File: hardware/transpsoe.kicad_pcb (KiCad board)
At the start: 2 copper layers, 102.2 x 51 mm, 107 parts, among them J1 AudioJack2_SwitchT, J10 AudioJack2_SwitchT, J11 AudioJack2_SwitchT, J12 Conn_01x08_Female, J13 Conn_01x08_Female, J14 Conn_01x08_Male, J15 Conn_01x08_Male, J2 AudioJack2_SwitchT, J3 AudioJack2_SwitchT, J4 AudioJack2_SwitchT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

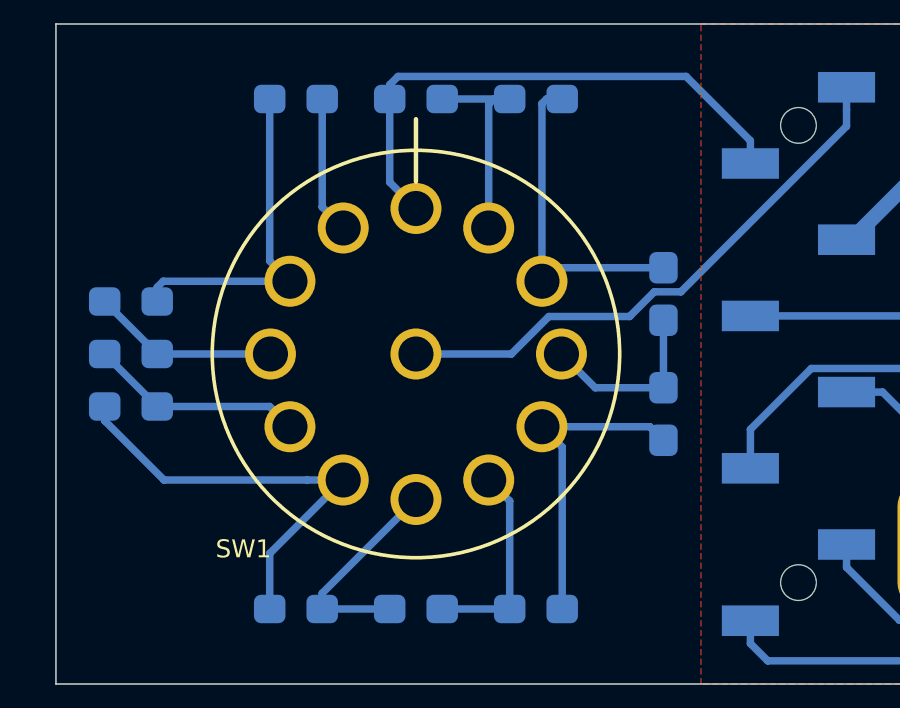
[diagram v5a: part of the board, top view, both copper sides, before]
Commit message: Increase annular ring size on rotary switch
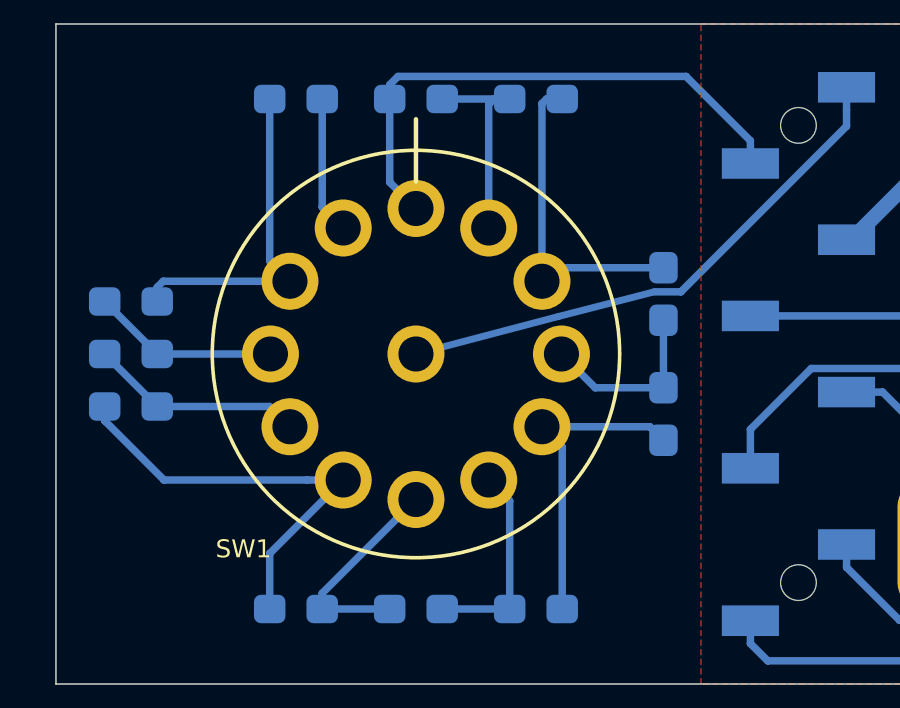
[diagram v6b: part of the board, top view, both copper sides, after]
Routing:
- net Jacks-SW1.a: track 18.8 -> 18.2 mm
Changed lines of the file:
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@@
     (thickness 1.6)
     (drawings 12)
-    (tracks 918)
+    (tracks 916)
     (zones 0)
     (modules 107)
@@
   )
   (setup
-    (last_trace_width 0.5)
+    (last_trace_width 0.25)
+    (user_trace_width 0.23)
     (user_trace_width 0.25)
     (user_trace_width 0.5)
@@
     (add_net SW1.b)
   )
+  (module transpsoe:MC12xxxCxx (layer F.Cu)
+    (at 112 111.25)
+    (descr "Half-inch Rotary Switch")
+    (fp_text reference SW1 (at -5.75 6.5) (layer F.SilkS)
+      (effects (font (size 0.6 0.6) (thickness 0.127)))
+    )
+    (fp_text value SW_Rotary12 (at 0 -9.25) (layer F.Fab)
+      (effects (font (size 1 1) (thickness 0.15)))
+    )
+    (fp_circle (center 0 0) (end -1.726323 -6.442725) (layer F.Fab) (width 0.1))
+    (fp_circle (center 0 0) (end -1.757381 -6.558636) (layer F.SilkS) (width 0.12))
+    (fp_circle (center 0 0) (end -1.822086 -6.800118) (layer F.CrtYd) (width 0.05))
+    (fp_line (start 0 -5.75) (end 0 -7.826787) (layer F.SilkS) (width 0.15))
+    (pad 1 thru_hole oval (at 0 -4.85 90) (size 1.9 1.9) (drill 1.17) (layers *.Cu *.Mask)
+      (net 78 Jacks-SW1.b))
+    (pad 2 thru_hole oval (at 2.424999 -4.200223 90) (size 1.9 1.9) (drill 1.17) (layers *.Cu *.Mask)
+      (net 47 "Net-(R81-Pad2)"))
+    (pad 3 thru_hole oval (at 4.200223 -2.425 90) (size 1.9 1.9) (drill 1.17) (layers *.Cu *.Mask)
+      (net 46 "Net-(R80-Pad2)"))
+    (pad 4 thru_hole oval (at 4.85 0 90) (size 1.9 1.9) (drill 1.17) (layers *.Cu *.Mask)
+      (net 45 "Net-(R79-Pad2)"))
+    (pad 5 thru_hole oval (at 4.200223 2.424999 90) (size 1.9 1.9) (drill 1.17) (layers *.Cu *.Mask)
+      (net 44 "Net-(R78-Pad2)"))
+    (pad 6 thru_hole oval (at 2.424999 4.200223 90) (size 1.9 1.9) (drill 1.17) (layers *.Cu *.Mask)
+      (net 43 "Net-(R77-Pad2)"))
+    (pad 7 thru_hole oval (at 0 4.85 90) (size 1.9 1.9) (drill 1.17) (layers *.Cu *.Mask)
+      (net 42 "Net-(R76-Pad2)"))
+    (pad 8 thru_hole oval (at -2.425 4.200223 90) (size 1.9 1.9) (drill 1.17) (layers *.Cu *.Mask)
+      (net 41 "Net-(R75-Pad2)"))
+    (pad 9 thru_hole oval (at -4.200223 2.425 90) (size 1.9 1.9) (drill 1.17) (layers *.Cu *.Mask)
+      (net 40 "Net-(R74-Pad2)"))
+    (pad 10 thru_hole oval (at -4.85 0 90) (size 1.9 1.9) (drill 1.17) (layers *.Cu *.Mask)
+      (net 39 "Net-(R73-Pad2)"))
+    (pad 11 thru_hole oval (at -4.200223 -2.425 90) (size 1.9 1.9) (drill 1.17) (layers *.Cu *.Mask)
+      (net 38 "Net-(R72-Pad2)"))
+    (pad 12 thru_hole oval (at -2.425 -4.200223 90) (size 1.9 1.9) (drill 1.17) (layers *.Cu *.Mask)
+      (net 37 "Net-(R72-Pad1)"))
+    (pad 13 thru_hole oval (at 0 0 90) (size 1.9 1.9) (drill 1.17) (layers *.Cu *.Mask)
+      (net 79 Jacks-SW1.a))
+    (model :transpsoe:MC12L1NCQD.stp
+      (offset (xyz 0 0 2.75))
+      (scale (xyz 1 1 1))
+      (rotate (xyz -90 0 0))
+    )
+  )
   (module Potentiometer_THT:Potentiometer_Bourns_3296W_Vertical (layer B.Cu)
     (at 133 90.25 180)
@@
     )
   )
-  (module transpsoe:MC12xxxCxx (layer F.Cu)
-    (at 112 111.25)
-    (descr "Half-inch Rotary Switch")
-    (fp_text reference SW1 (at -5.75 6.5) (layer F.SilkS)
-      (effects (font (size 0.6 0.6) (thickness 0.127)))
-    )
-    (fp_text value SW_Rotary12 (at 0 -9.25) (layer F.Fab)
-      (effects (font (size 1 1) (thickness 0.15)))
-    )
-    (fp_line (start 0 -5.75) (end 0 -7.826787) (layer F.SilkS) (width 0.15))
-    (fp_circle (center 0 0) (end -1.822086 -6.800118) (layer F.CrtYd) (width 0.05))
-    (fp_circle (center 0 0) (end -1.757381 -6.558636) (layer F.SilkS) (width 0.12))
-    (fp_circle (center 0 0) (end -1.726323 -6.442725) (layer F.Fab) (width 0.1))
-    (pad 13 thru_hole oval (at 0 0 285) (size 1.7 1.7) (drill 1.17) (layers *.Cu *.Mask)
-      (net 79 Jacks-SW1.a))
-    (pad 12 thru_hole oval (at -2.425 -4.200223 90) (size 1.7 1.7) (drill 1.17) (layers *.Cu *.Mask)
-      (net 37 "Net-(R72-Pad1)"))
-    (pad 11 thru_hole oval (at -4.200223 -2.425 90) (size 1.7 1.7) (drill 1.17) (layers *.Cu *.Mask)
-      (net 38 "Net-(R72-Pad2)"))
-    (pad 10 thru_hole oval (at -4.85 0 90) (size 1.7 1.7) (drill 1.17) (layers *.Cu *.Mask)
-      (net 39 "Net-(R73-Pad2)"))
-    (pad 9 thru_hole oval (at -4.200223 2.425 90) (size 1.7 1.7) (drill 1.17) (layers *.Cu *.Mask)
-      (net 40 "Net-(R74-Pad2)"))
-    (pad 8 thru_hole oval (at -2.425 4.200223 90) (size 1.7 1.7) (drill 1.17) (layers *.Cu *.Mask)
-      (net 41 "Net-(R75-Pad2)"))
-    (pad 7 thru_hole oval (at 0 4.85 90) (size 1.7 1.7) (drill 1.17) (layers *.Cu *.Mask)
-      (net 42 "Net-(R76-Pad2)"))
-    (pad 6 thru_hole oval (at 2.424999 4.200223 90) (size 1.7 1.7) (drill 1.17) (layers *.Cu *.Mask)
-      (net 43 "Net-(R77-Pad2)"))
-    (pad 5 thru_hole oval (at 4.200223 2.424999 90) (size 1.7 1.7) (drill 1.17) (layers *.Cu *.Mask)
-      (net 44 "Net-(R78-Pad2)"))
-    (pad 4 thru_hole oval (at 4.85 0 90) (size 1.7 1.7) (drill 1.17) (layers *.Cu *.Mask)
-      (net 45 "Net-(R79-Pad2)"))
-    (pad 3 thru_hole oval (at 4.200223 -2.425 90) (size 1.7 1.7) (drill 1.17) (layers *.Cu *.Mask)
-      (net 46 "Net-(R80-Pad2)"))
-    (pad 2 thru_hole oval (at 2.424999 -4.200223 90) (size 1.7 1.7) (drill 1.17) (layers *.Cu *.Mask)
-      (net 47 "Net-(R81-Pad2)"))
-    (pad 1 thru_hole oval (at 0 -4.85 90) (size 1.7 1.7) (drill 1.17) (layers *.Cu *.Mask)
-      (net 78 Jacks-SW1.b))
-    (model :transpsoe:MC12L1NCQD.stp
-      (offset (xyz 0 0 2.75))
-      (scale (xyz 1 1 1))
-      (rotate (xyz -90 0 0))
-    )
-  )
   (module transpsoe:raccoon-7.5 (layer B.Cu)
     (at 198.2 81.85 180)
@@
   (segment (start 108.875 106.349777) (end 109.575 107.049777) (width 0.25) (layer B.Cu) (net 37))
   (segment (start 108.875 102.75) (end 108.875 106.349777) (width 0.25) (layer B.Cu) (net 37))
-  (segment (start 107.125 108.150223) (end 107.799777 108.825) (width 0.25) (layer B.Cu) (net 38))
-  (segment (start 107.125 102.75) (end 107.125 108.150223) (width 0.25) (layer B.Cu) (net 38))
   (segment (start 103.575 108.825) (end 103.375 109.025) (width 0.25) (layer B.Cu) (net 38))
   (segment (start 103.375 109.025) (end 103.375 109.5) (width 0.25) (layer B.Cu) (net 38))
   (segment (start 107.799777 108.825) (end 103.575 108.825) (width 0.25) (layer B.Cu) (net 38))
+  (segment (start 107.125 108.150223) (end 107.799777 108.825) (width 0.25) (layer B.Cu) (net 38))
+  (segment (start 107.125 102.75) (end 107.125 108.150223) (width 0.25) (layer B.Cu) (net 38))
   (segment (start 101.625 109.5) (end 103.375 111.25) (width 0.25) (layer B.Cu) (net 39))
   (segment (start 103.375 111.25) (end 107.15 111.25) (width 0.25) (layer B.Cu) (net 39))
@@
   (segment (start 120.831912 109.17741) (end 126.3525 103.656822) (width 0.25) (layer B.Cu) (net 79))
   (segment (start 119.944396 109.17741) (end 120.831912 109.17741) (width 0.25) (layer B.Cu) (net 79))
-  (segment (start 119.121806 110) (end 119.944396 109.17741) (width 0.25) (layer B.Cu) (net 79))
-  (segment (start 116.431446 110) (end 119.121806 110) (width 0.25) (layer B.Cu) (net 79))
-  (segment (start 115.181446 111.25) (end 116.431446 110) (width 0.25) (layer B.Cu) (net 79))
-  (segment (start 112 111.25) (end 115.181446 111.25) (width 0.25) (layer B.Cu) (net 79))
+  (segment (start 112 111.25) (end 116.75 110) (width 0.23) (layer B.Cu) (net 79))
+  (segment (start 116.75 110) (end 119.944396 109.17741) (width 0.23) (layer B.Cu) (net 79))
   (segment (start 153.25 110.3) (end 153.25 110.5) (width 0.25) (layer B.Cu) (net 80))
   (segment (start 151 110.3) (end 153.25 110.3) (width 0.25) (layer B.Cu) (net 80))

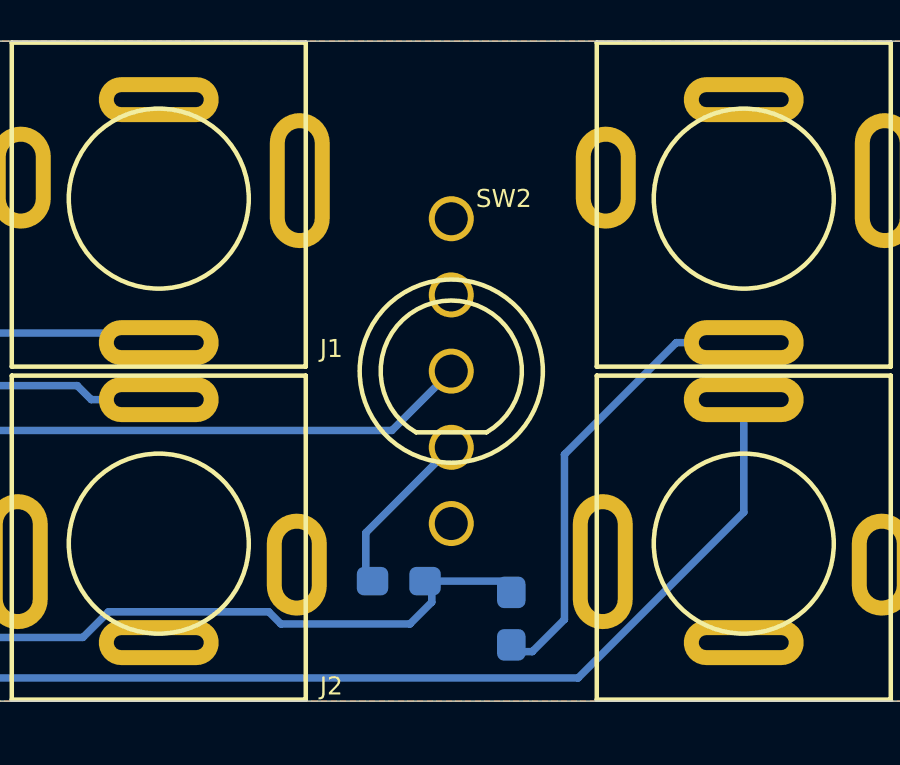
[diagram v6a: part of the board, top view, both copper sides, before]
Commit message: Correct orientation of summing switch
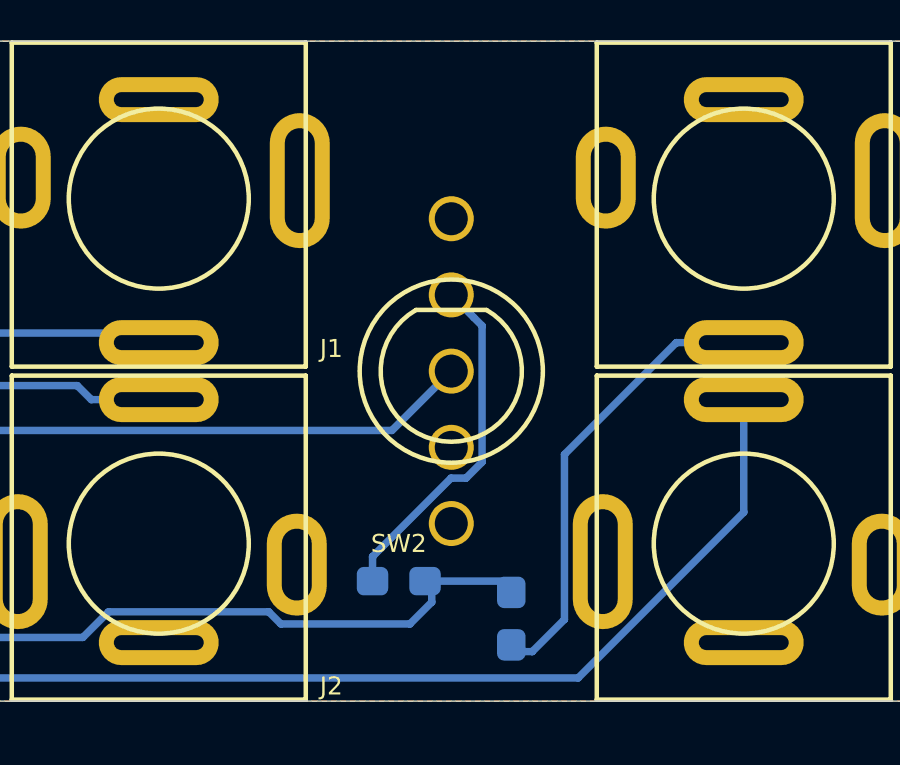
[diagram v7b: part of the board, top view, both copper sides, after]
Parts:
- turned SW2 to 0 degrees
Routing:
- net Net-(R16-Pad1): track 5.64 -> 11.8 mm
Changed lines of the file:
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@@
     (thickness 1.6)
     (drawings 12)
-    (tracks 916)
+    (tracks 921)
     (zones 0)
     (modules 107)
@@
   (page A4)
   (layers
-    (0 F.Cu signal)
+    (0 F.Cu signal hide)
     (31 B.Cu signal)
     (35 F.Paste user)
@@
   )
   (module transpsoe:BNT11SEA5QE (layer F.Cu)
-    (at 143.5 111.25 180)
+    (at 143.5 111.25)
     (descr "Sub-miniature toggle")
     (tags toggle)
@@
     (fp_arc (start 0 0) (end -1.175 -2.04) (angle -300.1) (layer F.SilkS) (width 0.15))
     (fp_line (start -1.175 -2.04) (end 1.175634 -2.039635) (layer F.SilkS) (width 0.15))
-    (pad 4 thru_hole circle (at 0 -5.08 180) (size 1.5 1.5) (drill 1.1) (layers *.Cu *.Mask))
-    (pad 4 thru_hole circle (at 0 5.08 180) (size 1.5 1.5) (drill 1.1) (layers *.Cu *.Mask))
-    (pad 3 thru_hole circle (at 0 -2.54 180) (size 1.5 1.5) (drill 1.1) (layers *.Cu *.Mask)
+    (pad 4 thru_hole circle (at 0 -5.08) (size 1.5 1.5) (drill 1.1) (layers *.Cu *.Mask))
+    (pad 4 thru_hole circle (at 0 5.08) (size 1.5 1.5) (drill 1.1) (layers *.Cu *.Mask))
+    (pad 3 thru_hole circle (at 0 -2.54) (size 1.5 1.5) (drill 1.1) (layers *.Cu *.Mask)
       (net 62 "Net-(R16-Pad1)"))
-    (pad 2 thru_hole circle (at 0 0 180) (size 1.5 1.5) (drill 1.1) (layers *.Cu *.Mask)
+    (pad 2 thru_hole circle (at 0 0) (size 1.5 1.5) (drill 1.1) (layers *.Cu *.Mask)
       (net 77 Jacks-SUM_SW.out))
-    (pad 1 thru_hole circle (at 0 2.54 180) (size 1.5 1.5) (drill 1.1) (layers *.Cu *.Mask)
+    (pad 1 thru_hole circle (at 0 2.54) (size 1.5 1.5) (drill 1.1) (layers *.Cu *.Mask)
       (net 93 "Net-(SW2-Pad1)"))
     (model :transpsoe:BNT11SEA5QE.wrl
@@
   (segment (start 155.15 75.5) (end 155 75.5) (width 0.25) (layer B.Cu) (net 61))
   (segment (start 155 75.35) (end 155.15 75.5) (width 0.25) (layer B.Cu) (net 61))
-  (segment (start 140.65 116.64) (end 143.5 113.79) (width 0.25) (layer B.Cu) (net 62))
-  (segment (start 140.65 118.25) (end 140.65 116.64) (width 0.25) (layer B.Cu) (net 62))
+  (segment (start 144.527401 109.737401) (end 144.249999 109.459999) (width 0.25) (layer B.Cu) (net 62))
+  (segment (start 144.527401 114.283153) (end 144.527401 109.737401) (width 0.25) (layer B.Cu) (net 62))
+  (segment (start 144.249999 109.459999) (end 143.5 108.71) (width 0.25) (layer B.Cu) (net 62))
+  (segment (start 143.993153 114.817401) (end 144.527401 114.283153) (width 0.25) (layer B.Cu) (net 62))
+  (segment (start 143.492045 114.817401) (end 143.993153 114.817401) (width 0.25) (layer B.Cu) (net 62))
+  (segment (start 140.875 117.434446) (end 143.492045 114.817401) (width 0.25) (layer B.Cu) (net 62))
+  (segment (start 140.875 118.25) (end 140.875 117.434446) (width 0.25) (layer B.Cu) (net 62))
   (segment (start 166.94 77.79) (end 166.4 77.25) (width 0.25) (layer B.Cu) (net 63))
   (segment (start 166.94 79.55) (end 166.94 77.79) (width 0.25) (layer B.Cu) (net 63))

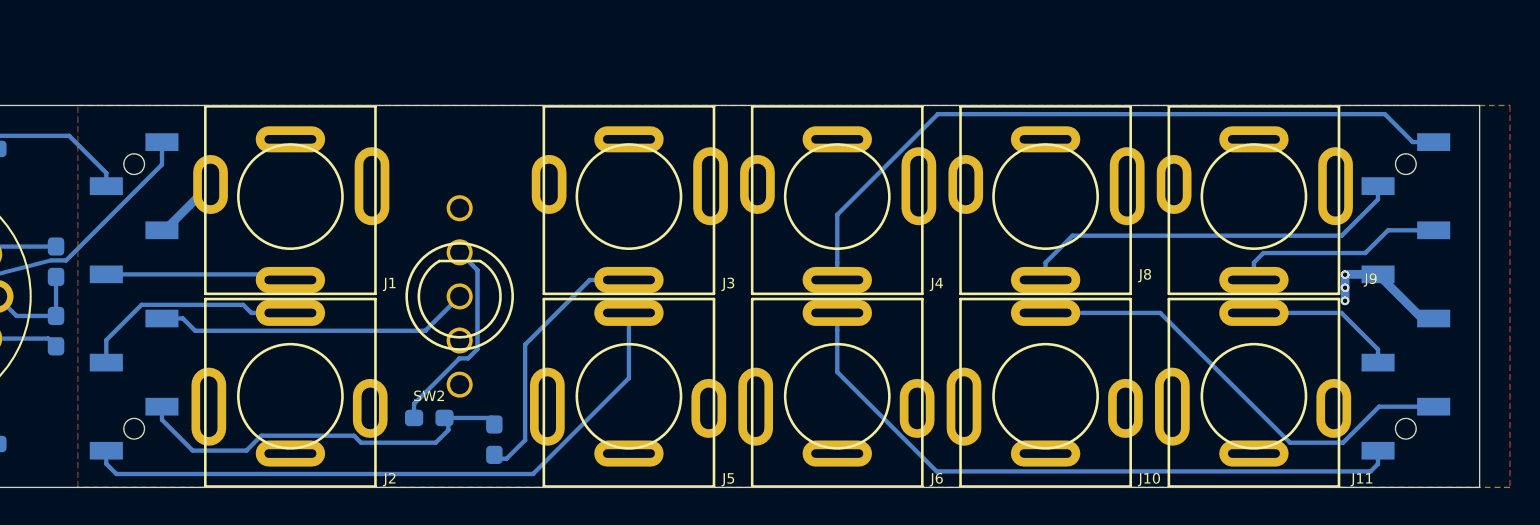
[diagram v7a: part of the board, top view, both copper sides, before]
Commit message: Push 3.5mm jacks 0.05mm closer to the edge
It's a very small nudge, and puts them more at risk of being slightly
off the board, but increases the tolerances for clearance between
adjacent jacks. We have ~0.5mm of clearance on the side of the board,
and this should only eat into at most 0.1mm of it.
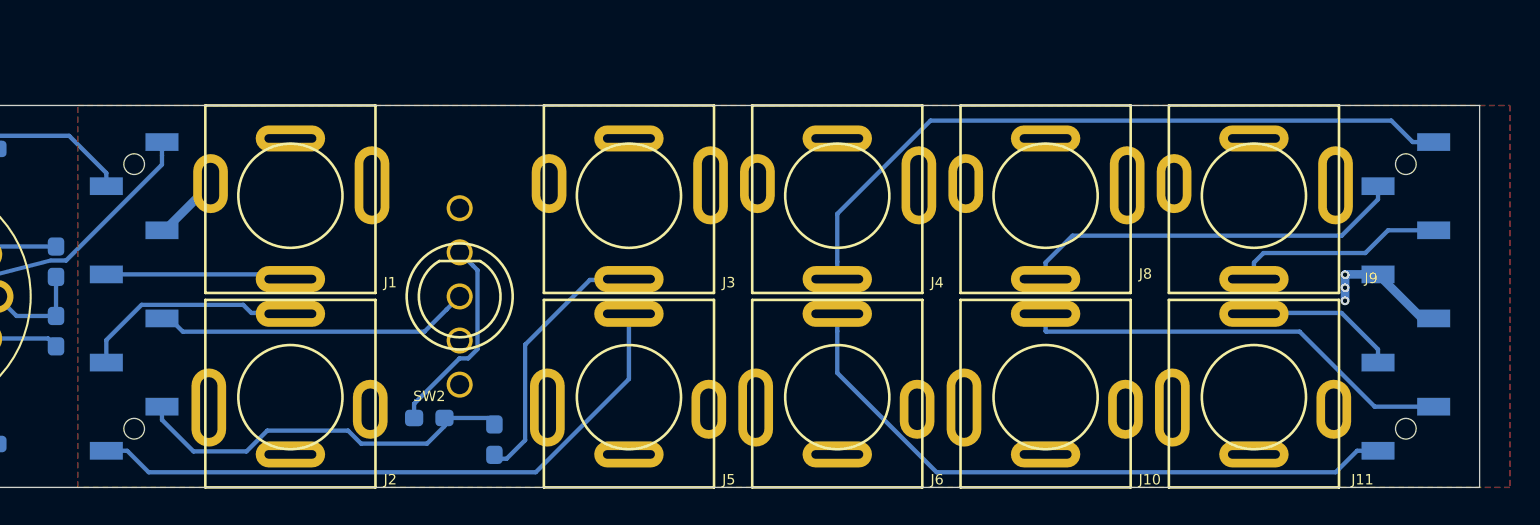
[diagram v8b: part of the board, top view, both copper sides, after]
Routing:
- net Jacks-J10.T: track 26.3 -> 25.2 mm
- net Jacks-J5.T: track 37.1 -> 36.6 mm
